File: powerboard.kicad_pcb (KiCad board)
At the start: 2 copper layers, 81.3 x 61.6 mm, 26 parts, among them J1 B03B, J2 EMER_SW, J3 EMER_SW, Q1 TJ60S04M3L, U1 TLP222A

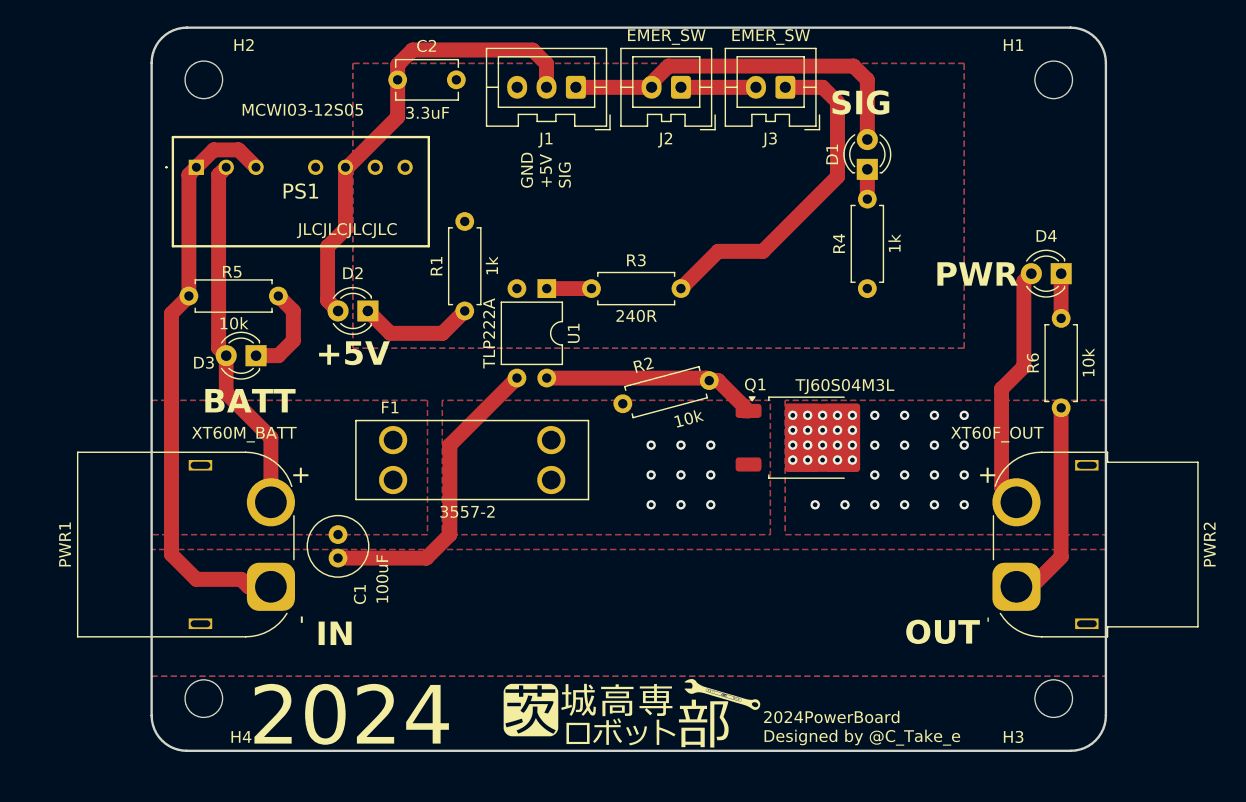
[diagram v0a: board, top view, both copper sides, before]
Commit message: pcb: make the outline wider, move holes
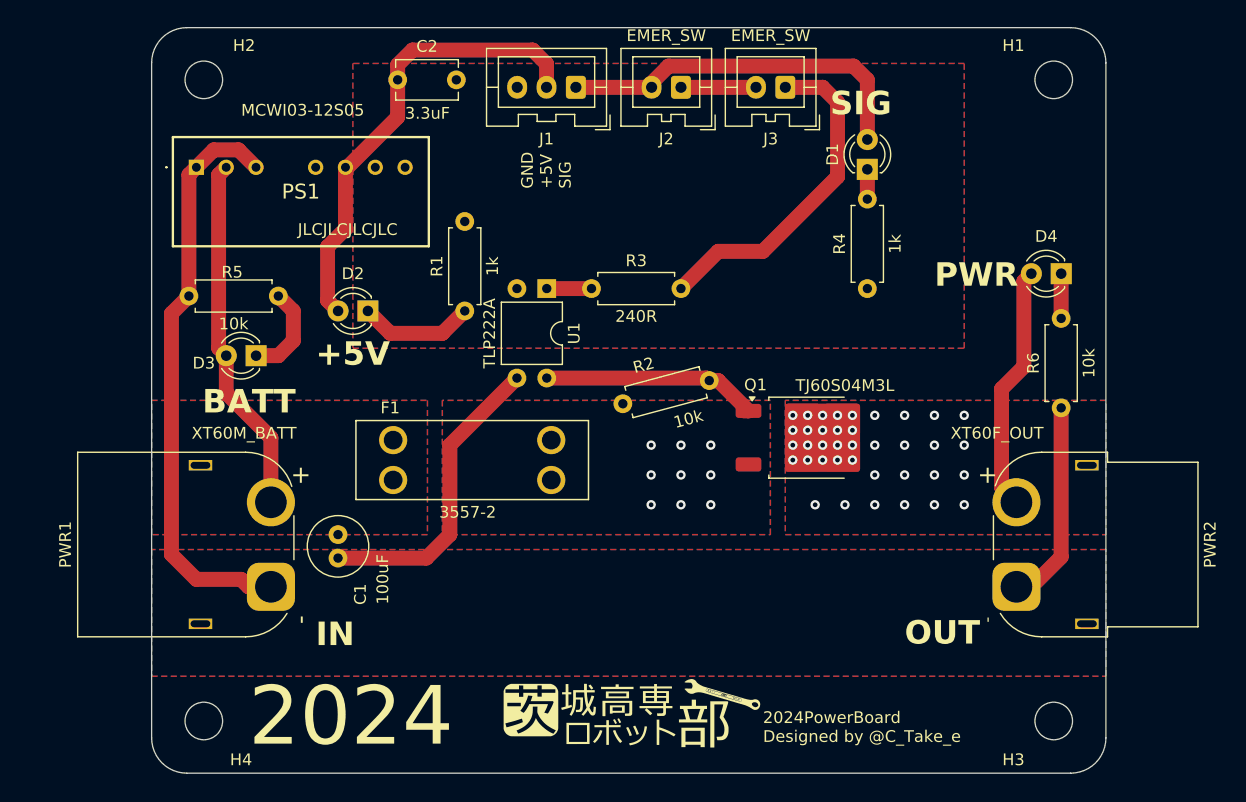
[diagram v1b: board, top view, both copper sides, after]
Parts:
- moved H3 1.91 mm to (192.4, 142.9)
- moved H4 1.91 mm to (120.0, 142.9)
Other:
- board size 81.3 x 61.6 mm -> 81.3 x 63.5 mm
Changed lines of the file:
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@@
 	(footprint "MountingHole:MountingHole_3.2mm_M3"
 		(layer "F.Cu")
-		(at 192.405 140.97)
+		(at 192.405 142.875)
 		(descr "Mounting Hole 3.2mm, no annular, M3")
 		(tags "mounting hole 3.2mm no annular m3")
@@
 	(footprint "MountingHole:MountingHole_3.2mm_M3"
 		(layer "F.Cu")
-		(at 120.015 140.97)
+		(at 120.015 142.875)
 		(descr "Mounting Hole 3.2mm, no annular, M3")
 		(tags "mounting hole 3.2mm no annular m3")
@@
 	)
 	(gr_arc
-		(start 196.85 142.415)
-		(mid 195.97132 144.53632)
-		(end 193.85 145.415)
+		(start 115.57 86.82)
+		(mid 116.44868 84.69868)
+		(end 118.57 83.82)
 		(stroke
-			(width 0.2)
+			(width 0.1)
 			(type default)
 		)
 		(layer "Edge.Cuts")
 	)
-	(gr_arc
-		(start 115.57 86.82)
-		(mid 116.44868 84.69868)
-		(end 118.57 83.82)
+	(gr_line
+		(start 196.85 86.82)
+		(end 196.85 144.32)
 		(stroke
-			(width 0.2)
+			(width 0.1)
 			(type default)
 		)
@@
 	)
 	(gr_arc
-		(start 193.85 83.82)
-		(mid 195.97132 84.69868)
-		(end 196.85 86.82)
+		(start 118.57 147.32)
+		(mid 116.44868 146.44132)
+		(end 115.57 144.32)
 		(stroke
-			(width 0.2)
+			(width 0.1)
 			(type default)
 		)
@@
 	)
 	(gr_line
-		(start 118.57 83.82)
-		(end 193.85 83.82)
+		(start 115.57 144.32)
+		(end 115.57 86.82)
 		(stroke
-			(width 0.2)
+			(width 0.1)
 			(type default)
 		)
@@
 	)
 	(gr_arc
-		(start 118.57 145.415)
-		(mid 116.44868 144.53632)
-		(end 115.57 142.415)
+		(start 196.85 144.32)
+		(mid 195.97132 146.44132)
+		(end 193.85 147.32)
 		(stroke
-			(width 0.2)
+			(width 0.1)
 			(type default)
 		)
@@
 	)
 	(gr_line
-		(start 115.57 142.415)
-		(end 115.57 86.82)
+		(start 193.85 147.32)
+		(end 118.57 147.32)
 		(stroke
-			(width 0.2)
+			(width 0.1)
 			(type default)
 		)
 		(layer "Edge.Cuts")
 	)
-	(gr_line
-		(start 193.85 145.415)
-		(end 118.57 145.415)
+	(gr_arc
+		(start 193.85 83.82)
+		(mid 195.97132 84.69868)
+		(end 196.85 86.82)
 		(stroke
-			(width 0.2)
+			(width 0.1)
 			(type default)
 		)
@@
 	)
 	(gr_line
-		(start 196.85 86.82)
-		(end 196.85 142.415)
+		(start 118.57 83.82)
+		(end 193.85 83.82)
 		(stroke
-			(width 0.2)
+			(width 0.1)
 			(type default)
 		)
@@
 		(layer "Cmts.User")
 		(pts
-			(xy 193.85 83.82) (xy 193.85 145.415)
+			(xy 196.85 83.82) (xy 196.85 147.32)
 		)
-		(height -17.605)
-		(gr_text "61.5950 mm"
-			(at 210.305 114.6175 90)
+		(height -16.51)
+		(gr_text "63.5000 mm"
+			(at 212.21 115.57 90)
 			(layer "Cmts.User")
 			(effects

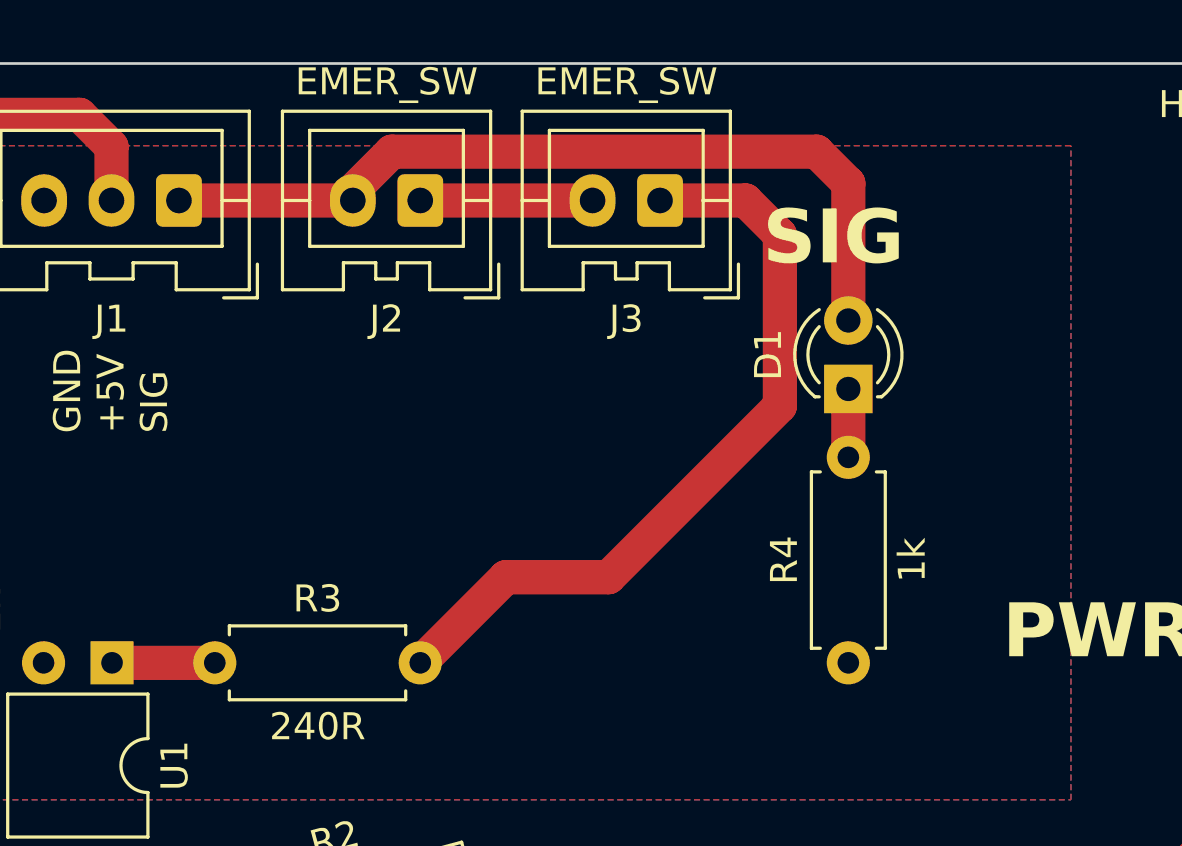
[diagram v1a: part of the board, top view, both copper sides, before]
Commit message: pcb: Leave space between J1, J2, and J3
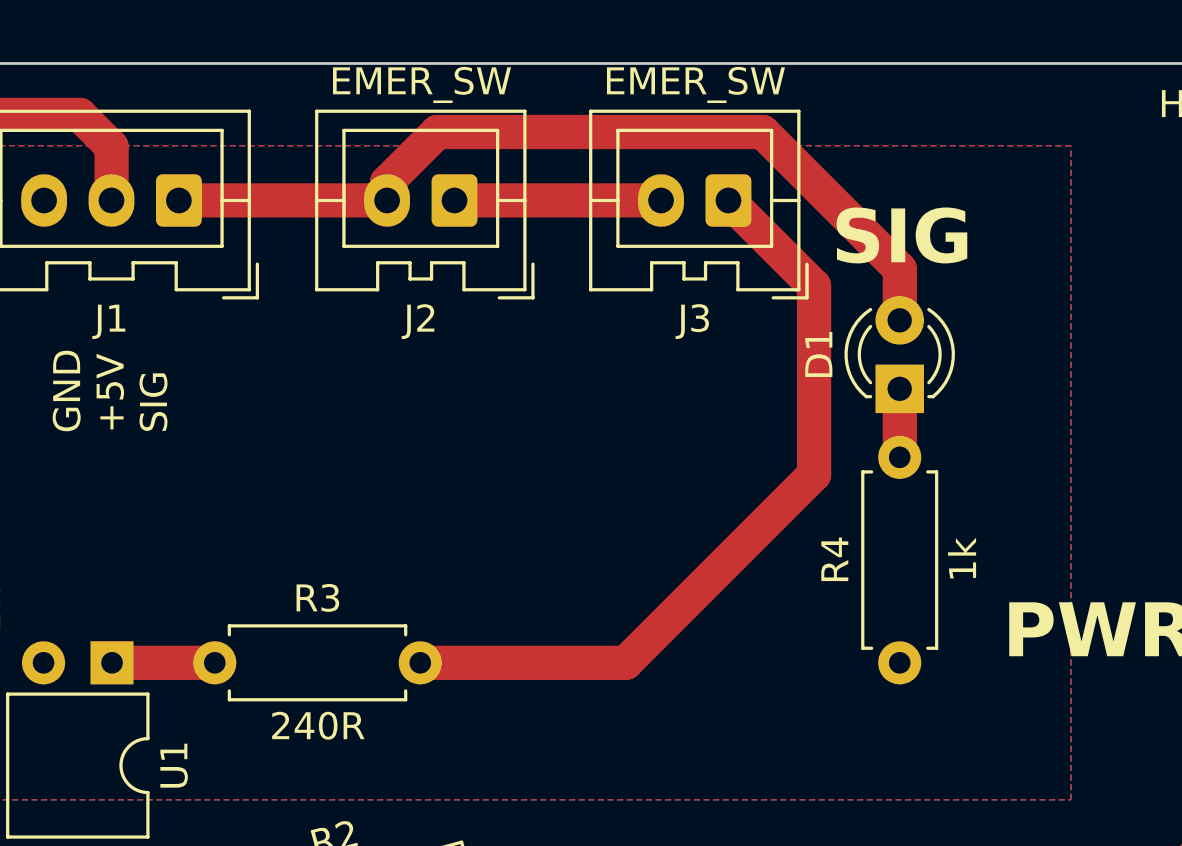
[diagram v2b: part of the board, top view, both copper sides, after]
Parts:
- moved J3 2.54 mm to (172.1, 88.9)
- moved D1 1.91 mm to (178.4, 95.9)
- moved R4 1.91 mm to (178.4, 98.4)
- moved J2 1.27 mm to (161.9, 88.9)
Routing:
- net Net-(J2-Pin_1): track 6.39 -> 7.66 mm
- net sig: track 31.4 -> 32.2 mm

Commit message: pcb/sch: Add FET
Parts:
- added Q2: TJ60S04M3L, Package_TO_SOT_SMD:TO-252-2, F.Cu at (170.2, 123.8)
- added R7: 10k, Resistor_THT:R_Axial_DIN0207_L6.3mm_D2.5mm_P7.62mm_Horizontal, F.Cu at (161.9, 126.4)
- moved Q1 2.84 mm to (170.2, 116.2)
- moved R2 1.40 mm to (154.3, 115.9)
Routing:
- net FET_G: track 18.8 -> 26.2 mm
- net VOUT: vias 38 -> 16

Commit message: Revert "pcb/sch: Add FET"
This reverts commit 0032eebc1d6eb9ed2a957a3795ce5049efafd74e.
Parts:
- removed Q2: TJ60S04M3L, Package_TO_SOT_SMD:TO-252-2
- removed R7: 10k, Resistor_THT:R_Axial_DIN0207_L6.3mm_D2.5mm_P7.62mm_Horizontal
- moved Q1 2.84 mm to (171.4, 118.7)
- moved R2 1.40 mm to (155.7, 115.9)
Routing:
- net FET_G: track 26.2 -> 18.8 mm
- net VOUT: vias 16 -> 38

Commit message: pcb: Delete vias under FET
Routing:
- net VOUT: vias 38 -> 18

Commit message: pcb: Delete vias under a FET
This reverts commit e1503daf84bd5df3be65f05229be8e469e7dccfe.
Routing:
- net VOUT: vias 18 -> 38

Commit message: pcb: BIG VOUT
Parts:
- moved Q1 9.55 mm to (161.9, 119.4)
- moved R2 6.49 mm to (149.2, 116.2), turned to 20 degrees
- moved R1 5.72 mm to (142.2, 102.2)
- moved F1 5.08 mm to (137.8, 120.7)
- moved PWR1 2.54 mm to (123.2, 131.4)
- moved U1 2.54 mm to (146.7, 106.0)
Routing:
- net GNDPWR: track 93.4 -> 87.7 mm
- net FET_G: track 18.8 -> 14.1 mm
- net Net-(R3-Pad2): track 3.81 -> 6.35 mm
- net Net-(D2-K): track 9.83 -> 11.0 mm
- net BATT: track 31.4 -> 30.2 mm
- net VOUT: vias 38 -> 35
- net VDD: vias 9 -> 6

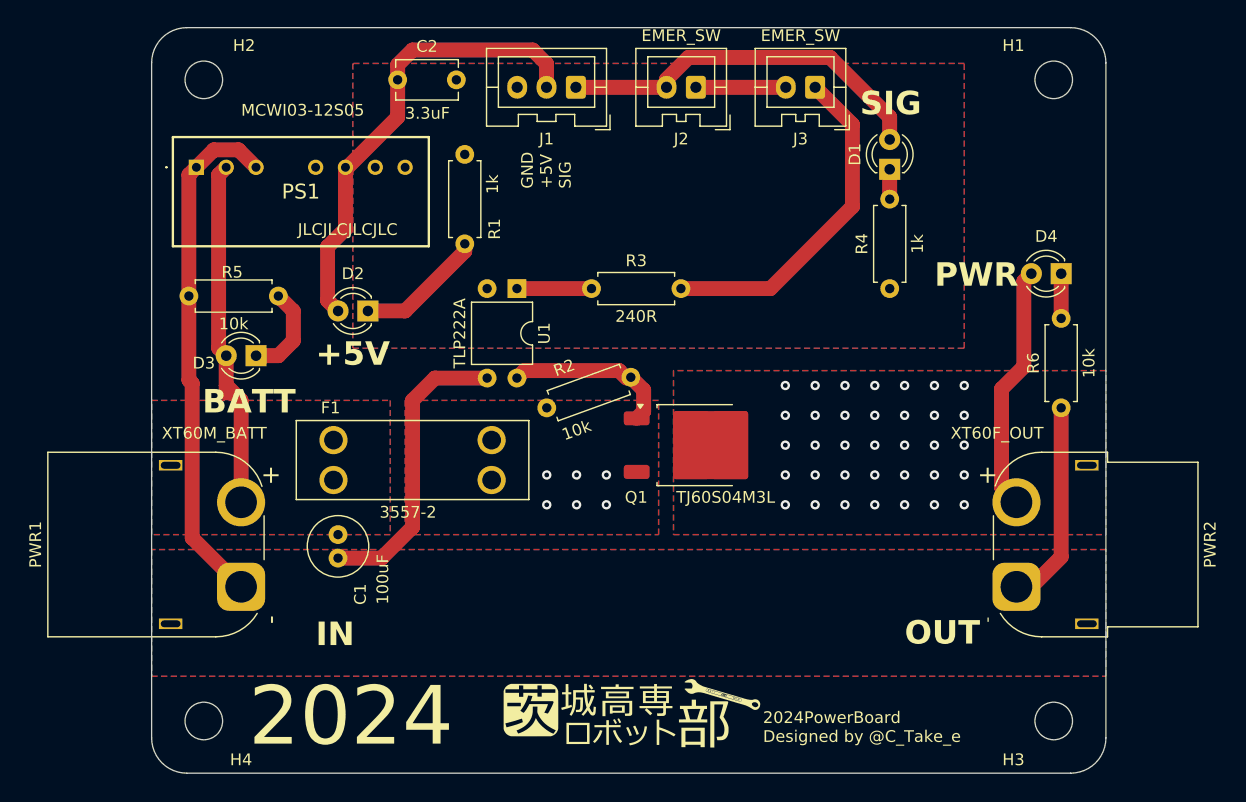
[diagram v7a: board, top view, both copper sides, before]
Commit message: pcb: BIGGER VOUT
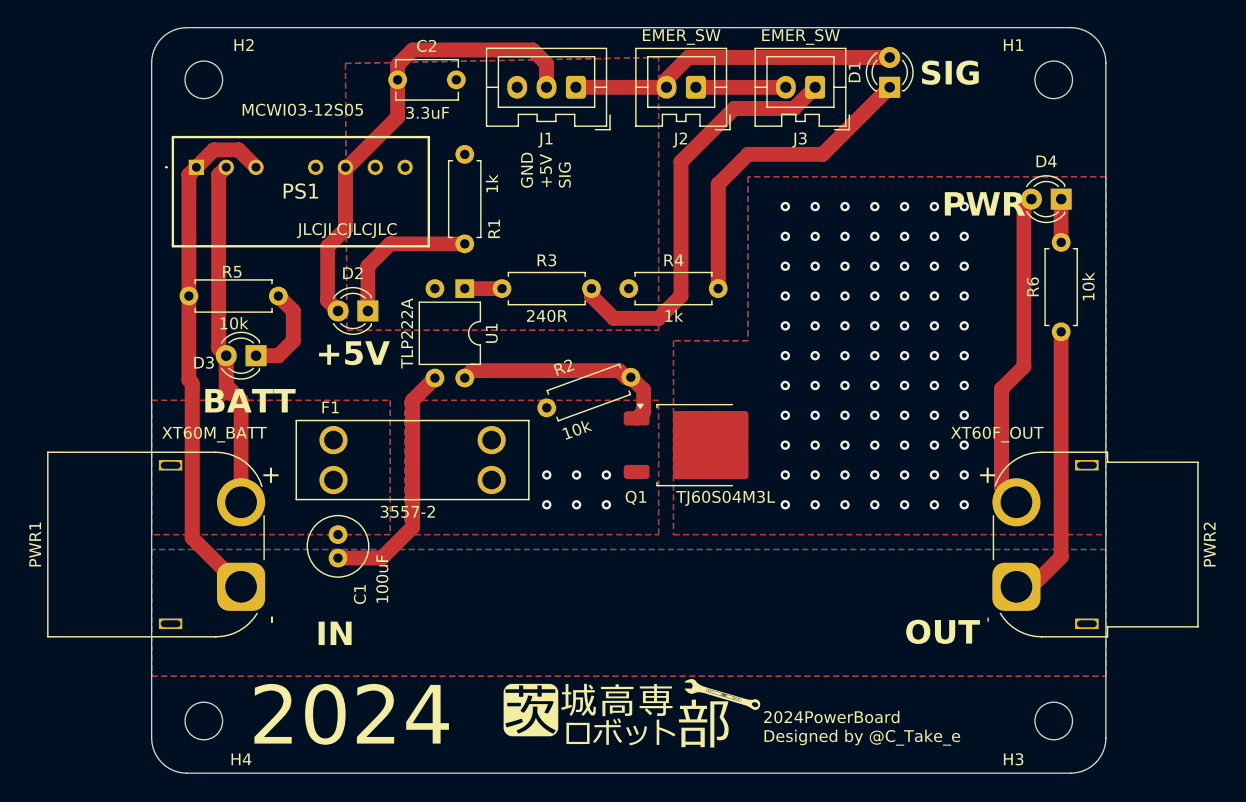
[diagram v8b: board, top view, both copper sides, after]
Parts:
- moved R4 16.5 mm to (163.8, 106.0), turned to 180 degrees
- moved R3 7.62 mm to (153.0, 106.0)
- moved D1 6.98 mm to (178.4, 88.9)
- moved R6 6.48 mm to (193.0, 102.1)
- moved D4 6.35 mm to (193.0, 98.4)
- moved U1 4.44 mm to (142.2, 106.0)
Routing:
- net Net-(D1-K): track 2.54 -> 26.9 mm
- net Net-(J3-Pin_1): track 29.0 -> 35.3 mm
- net VOUT: track 21.0 -> 27.4 mm, vias 35 -> 77
- net FET_G: track 14.1 -> 18.5 mm
- net sig: track 32.2 -> 28.2 mm
- net Net-(R3-Pad2): track 6.35 -> 3.17 mm
- net GNDPWR: track 87.7 -> 89.8 mm
- net Net-(D2-K): track 11.0 -> 12.9 mm
